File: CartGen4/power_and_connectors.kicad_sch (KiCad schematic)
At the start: 34 parts, among them J2 Conn_01x06_Male, U1 TPS65266-1RHBR

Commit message: Forgot to close footprint assignment tool
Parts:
- J2: footprint SamacSys_Parts:Pads_1x6_P2.54mm -> (none)
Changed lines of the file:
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@@
     (property "Reference" "J2" (id 0) (at 43.815 162.56 0))
     (property "Value" "Conn_01x06_Male" (id 1) (at 43.815 165.1 0))
-    (property "Footprint" "SamacSys_Parts:Pads_1x6_P2.54mm" (id 2) (at 43.18 172.72 0)
+    (property "Footprint" "" (id 2) (at 43.18 172.72 0)
       (effects (font (size 1.27 1.27)) hide)
     )

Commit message: Made general component placement + fixed ADDR
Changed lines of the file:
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@@
     )
   )
-  (global_label "GB_ADDR_5V[0..7]" (shape input) (at 193.04 71.12 180) (fields_autoplaced)
+  (global_label "GB_DATA_5V[0..7]" (shape input) (at 193.04 71.12 180) (fields_autoplaced)
     (effects (font (size 1.27 1.27)) (justify right))
-    (property "Intersheet References" "${INTERSHEET_REFS}" (id 0) (at 173.6331 71.0406 0)
+    (property "Intersheet References" "${INTERSHEET_REFS}" (id 0) (at 174.1169 71.0406 0)
       (effects (font (size 1.27 1.27)) (justify right) hide)
     )

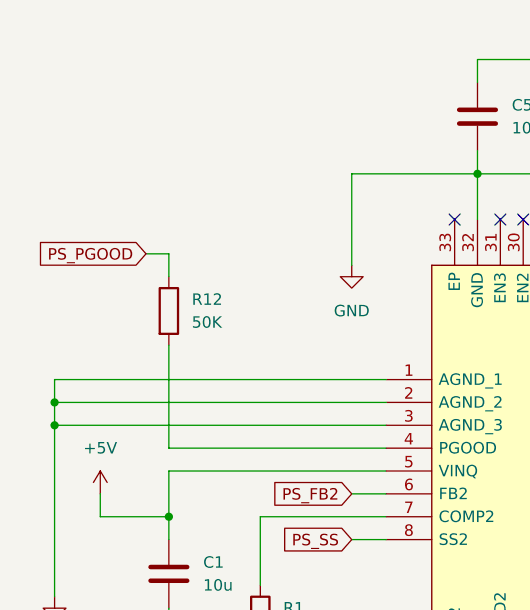
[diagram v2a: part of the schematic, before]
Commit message: Fixed PS_PGOOD pullup
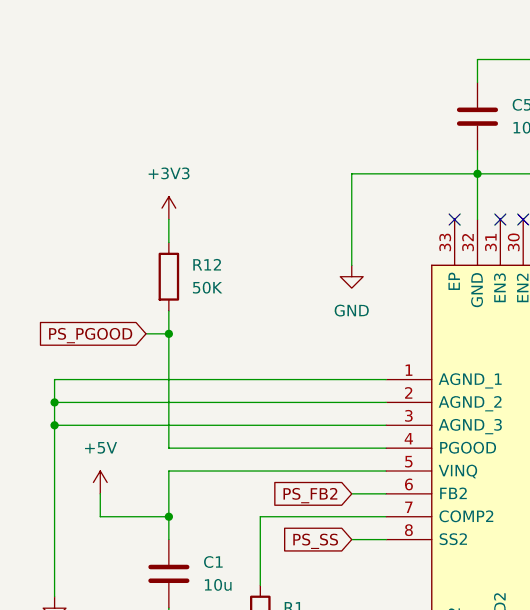
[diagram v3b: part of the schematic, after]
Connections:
- net +3V3: now also R12.1
- net PS_PGOOD: now also R12.2, U1.4 (PGOOD); no longer R12.1
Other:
- moved on the sheet: R12
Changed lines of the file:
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@@
   (junction (at 97.79 31.75) (diameter 0) (color 0 0 0 0)
+  )
+  (junction (at 43.18 62.23) (diameter 0) (color 0 0 0 0)
   )
   (junction (at 137.16 107.95) (diameter 0) (color 0 0 0 0)
@@
     (stroke (width 0) (type default) (color 0 0 0 0))
   )
-  (wire (pts (xy 43.18 74.93) (xy 43.18 63.5))
+  (wire (pts (xy 43.18 74.93) (xy 43.18 62.23))
     (stroke (width 0) (type default) (color 0 0 0 0))
   )
@@
     (stroke (width 0) (type default) (color 0 0 0 0))
   )
-  (wire (pts (xy 43.18 55.88) (xy 43.18 53.34))
-    (stroke (width 0) (type default) (color 0 0 0 0))
-  )
   (wire (pts (xy 120.65 41.91) (xy 120.65 44.45))
     (stroke (width 0) (type default) (color 0 0 0 0))
@@
     (stroke (width 0) (type default) (color 0 0 0 0))
   )
+  (wire (pts (xy 43.18 62.23) (xy 43.18 59.69))
+    (stroke (width 0) (type default) (color 0 0 0 0))
+  )
+  (wire (pts (xy 40.64 62.23) (xy 43.18 62.23))
+    (stroke (width 0) (type default) (color 0 0 0 0))
+  )
   (bus (pts (xy 217.17 82.55) (xy 217.17 80.01))
     (stroke (width 0) (type default) (color 0 0 0 0))
@@
     (stroke (width 0) (type default) (color 0 0 0 0))
   )
-  (wire (pts (xy 43.18 53.34) (xy 40.64 53.34))
-    (stroke (width 0) (type default) (color 0 0 0 0))
-  )
   (wire (pts (xy 212.09 123.19) (xy 247.65 123.19))
     (stroke (width 0) (type default) (color 0 0 0 0))
@@
   )
   (wire (pts (xy 102.87 80.01) (xy 106.68 80.01))
+    (stroke (width 0) (type default) (color 0 0 0 0))
+  )
+  (wire (pts (xy 43.18 49.53) (xy 43.18 52.07))
     (stroke (width 0) (type default) (color 0 0 0 0))
   )
@@
     )
   )
-  (global_label "PS_PGOOD" (shape input) (at 40.64 53.34 180) (fields_autoplaced)
+  (global_label "PS_PGOOD" (shape input) (at 40.64 62.23 180) (fields_autoplaced)
     (effects (font (size 1.27 1.27)) (justify right))
-    (property "Intersheet References" "${INTERSHEET_REFS}" (id 0) (at 28.3088 53.2606 0)
+    (property "Intersheet References" "${INTERSHEET_REFS}" (id 0) (at 28.3088 62.1506 0)
       (effects (font (size 1.27 1.27)) (justify right) hide)
     )
@@
     )
     (property "Datasheet" "" (id 3) (at 82.55 130.81 0)
+      (effects (font (size 1.27 1.27)) hide)
+    )
+    (pin "1")
+  )
+  (symbol (lib_id "power:+3V3") (at 43.18 49.53 0) (unit 1)
+    (in_bom yes) (on_board yes) (fields_autoplaced)
+    (property "Reference" "#PWR?" (id 0) (at 43.18 53.34 0)
+      (effects (font (size 1.27 1.27)) hide)
+    )
+    (property "Value" "+3V3" (id 1) (at 43.18 44.45 0))
+    (property "Footprint" "" (id 2) (at 43.18 49.53 0)
+      (effects (font (size 1.27 1.27)) hide)
+    )
+    (property "Datasheet" "" (id 3) (at 43.18 49.53 0)
       (effects (font (size 1.27 1.27)) hide)
     )
@@
     (pin "2")
   )
-  (symbol (lib_id "Device:R") (at 43.18 59.69 0) (unit 1)
+  (symbol (lib_id "Device:R") (at 43.18 55.88 0) (unit 1)
     (in_bom yes) (on_board yes) (fields_autoplaced)
-    (property "Reference" "R12" (id 0) (at 45.72 58.4199 0)
+    (property "Reference" "R12" (id 0) (at 45.72 54.6099 0)
       (effects (font (size 1.27 1.27)) (justify left))
     )
-    (property "Value" "50K" (id 1) (at 45.72 60.9599 0)
+    (property "Value" "50K" (id 1) (at 45.72 57.1499 0)
       (effects (font (size 1.27 1.27)) (justify left))
     )
-    (property "Footprint" "Resistor_SMD:R_0603_1608Metric_Pad0.98x0.95mm_HandSolder" (id 2) (at 41.402 59.69 90)
-      (effects (font (size 1.27 1.27)) hide)
-    )
-    (property "Datasheet" "~" (id 3) (at 43.18 59.69 0)
-      (effects (font (size 1.27 1.27)) hide)
-    )
-    (property "Tolerance" "10%" (id 4) (at 43.18 59.69 0)
-      (effects (font (size 1.27 1.27)) hide)
-    )
-    (property "Source" "ANY" (id 5) (at 43.18 59.69 0)
-      (effects (font (size 1.27 1.27)) hide)
-    )
-    (property "Critical" "Y" (id 6) (at 43.18 59.69 0)
-      (effects (font (size 1.27 1.27)) hide)
-    )
+    (property "Footprint" "Resistor_SMD:R_0603_1608Metric_Pad0.98x0.95mm_HandSolder" (id 2) (at 41.402 55.88 90)
+      (effects (font (size 1.27 1.27)) hide)
+    )
+    (property "Datasheet" "~" (id 3) (at 43.18 55.88 0)
+      (effects (font (size 1.27 1.27)) hide)
+    )
+    (property "Tolerance" "10%" (id 4) (at 43.18 55.88 0)
+      (effects (font (size 1.27 1.27)) hide)
+    )
+    (property "Source" "ANY" (id 5) (at 43.18 55.88 0)
+      (effects (font (size 1.27 1.27)) hide)
+    )
+    (property "Critical" "Y" (id 6) (at 43.18 55.88 0)
+      (effects (font (size 1.27 1.27)) hide)
+    )

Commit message: Changed most R and C to 0402 size
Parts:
- C11, C14, C17, C2, C3, C4, C9: footprint Capacitor_SMD:C_0603_1608Metric_Pad1.08x0.95mm_HandSolder -> Capacitor_SMD:C_0402_1005Metric_Pad0.74x0.62mm_HandSolder
- R1, R10, R12, R2, R3, R4, R5, R6, R7, R8, R9: footprint Resistor_SMD:R_0603_1608Metric_Pad0.98x0.95mm_HandSolder -> Resistor_SMD:R_0402_1005Metric_Pad0.72x0.64mm_HandSolder
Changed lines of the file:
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@@
       (effects (font (size 1.27 1.27)) (justify left))
     )
-    (property "Footprint" "Resistor_SMD:R_0603_1608Metric_Pad0.98x0.95mm_HandSolder" (id 2) (at 136.652 83.82 90)
+    (property "Footprint" "Resistor_SMD:R_0402_1005Metric_Pad0.72x0.64mm_HandSolder" (id 2) (at 136.652 83.82 90)
       (effects (font (size 1.27 1.27)) hide)
     )
@@
       (effects (font (size 1.27 1.27)) (justify left))
     )
-    (property "Footprint" "Capacitor_SMD:C_0603_1608Metric_Pad1.08x0.95mm_HandSolder" (id 2) (at 70.8152 115.57 0)
+    (property "Footprint" "Capacitor_SMD:C_0402_1005Metric_Pad0.74x0.62mm_HandSolder" (id 2) (at 70.8152 115.57 0)
       (effects (font (size 1.27 1.27)) hide)
     )
@@
       (effects (font (size 1.27 1.27)) (justify left))
     )
-    (property "Footprint" "Capacitor_SMD:C_0603_1608Metric_Pad1.08x0.95mm_HandSolder" (id 2) (at 110.1852 105.41 0)
+    (property "Footprint" "Capacitor_SMD:C_0402_1005Metric_Pad0.74x0.62mm_HandSolder" (id 2) (at 110.1852 105.41 0)
       (effects (font (size 1.27 1.27)) hide)
     )
@@
   (symbol (lib_id "power:+3V3") (at 43.18 49.53 0) (unit 1)
     (in_bom yes) (on_board yes) (fields_autoplaced)
-    (property "Reference" "#PWR?" (id 0) (at 43.18 53.34 0)
+    (property "Reference" "#PWR0102" (id 0) (at 43.18 53.34 0)
       (effects (font (size 1.27 1.27)) hide)
     )
@@
       (effects (font (size 1.27 1.27)) (justify left))
     )
-    (property "Footprint" "Resistor_SMD:R_0603_1608Metric_Pad0.98x0.95mm_HandSolder" (id 2) (at 130.302 50.8 90)
+    (property "Footprint" "Resistor_SMD:R_0402_1005Metric_Pad0.72x0.64mm_HandSolder" (id 2) (at 130.302 50.8 90)
       (effects (font (size 1.27 1.27)) hide)
     )
@@
       (effects (font (size 1.27 1.27)) (justify left))
     )
-    (property "Footprint" "Resistor_SMD:R_0603_1608Metric_Pad0.98x0.95mm_HandSolder" (id 2) (at 41.402 55.88 90)
+    (property "Footprint" "Resistor_SMD:R_0402_1005Metric_Pad0.72x0.64mm_HandSolder" (id 2) (at 41.402 55.88 90)
       (effects (font (size 1.27 1.27)) hide)
     )
@@
       (effects (font (size 1.27 1.27)) (justify left))
     )
-    (property "Footprint" "Capacitor_SMD:C_0603_1608Metric_Pad1.08x0.95mm_HandSolder" (id 2) (at 129.2352 92.71 0)
+    (property "Footprint" "Capacitor_SMD:C_0402_1005Metric_Pad0.74x0.62mm_HandSolder" (id 2) (at 129.2352 92.71 0)
       (effects (font (size 1.27 1.27)) hide)
     )
@@
     (property "Reference" "R8" (id 0) (at 147.32 63.5 90))
     (property "Value" "39K" (id 1) (at 147.32 66.04 90))
-    (property "Footprint" "Resistor_SMD:R_0603_1608Metric_Pad0.98x0.95mm_HandSolder" (id 2) (at 147.32 71.628 90)
+    (property "Footprint" "Resistor_SMD:R_0402_1005Metric_Pad0.72x0.64mm_HandSolder" (id 2) (at 147.32 71.628 90)
       (effects (font (size 1.27 1.27)) hide)
     )
@@
       (effects (font (size 1.27 1.27)) (justify left))
     )
-    (property "Footprint" "Capacitor_SMD:C_0603_1608Metric_Pad1.08x0.95mm_HandSolder" (id 2) (at 44.1452 135.89 0)
+    (property "Footprint" "Capacitor_SMD:C_0402_1005Metric_Pad0.74x0.62mm_HandSolder" (id 2) (at 44.1452 135.89 0)
       (effects (font (size 1.27 1.27)) hide)
     )
@@
       (effects (font (size 1.27 1.27)) (justify left))
     )
-    (property "Footprint" "Capacitor_SMD:C_0603_1608Metric_Pad1.08x0.95mm_HandSolder" (id 2) (at 154.6352 80.01 0)
+    (property "Footprint" "Capacitor_SMD:C_0402_1005Metric_Pad0.74x0.62mm_HandSolder" (id 2) (at 154.6352 80.01 0)
       (effects (font (size 1.27 1.27)) hide)
     )
@@
       (effects (font (size 1.27 1.27)) (justify left))
     )
-    (property "Footprint" "Capacitor_SMD:C_0603_1608Metric_Pad1.08x0.95mm_HandSolder" (id 2) (at 54.3052 107.95 0)
+    (property "Footprint" "Capacitor_SMD:C_0402_1005Metric_Pad0.74x0.62mm_HandSolder" (id 2) (at 54.3052 107.95 0)
       (effects (font (size 1.27 1.27)) hide)
     )
@@
       (effects (font (size 1.27 1.27)) (justify left))
     )
-    (property "Footprint" "Resistor_SMD:R_0603_1608Metric_Pad0.98x0.95mm_HandSolder" (id 2) (at 130.302 38.1 90)
+    (property "Footprint" "Resistor_SMD:R_0402_1005Metric_Pad0.72x0.64mm_HandSolder" (id 2) (at 130.302 38.1 90)
       (effects (font (size 1.27 1.27)) hide)
     )
@@
       (effects (font (size 1.27 1.27)) (justify left))
     )
-    (property "Footprint" "Resistor_SMD:R_0603_1608Metric_Pad0.98x0.95mm_HandSolder" (id 2) (at 156.972 114.3 90)
+    (property "Footprint" "Resistor_SMD:R_0402_1005Metric_Pad0.72x0.64mm_HandSolder" (id 2) (at 156.972 114.3 90)
       (effects (font (size 1.27 1.27)) hide)
     )
@@
     (property "Reference" "R4" (id 0) (at 121.92 85.09 90))
     (property "Value" "100K" (id 1) (at 121.92 87.63 90))
-    (property "Footprint" "Resistor_SMD:R_0603_1608Metric_Pad0.98x0.95mm_HandSolder" (id 2) (at 121.92 84.328 90)
+    (property "Footprint" "Resistor_SMD:R_0402_1005Metric_Pad0.72x0.64mm_HandSolder" (id 2) (at 121.92 84.328 90)
       (effects (font (size 1.27 1.27)) hide)
     )
@@
       (effects (font (size 1.27 1.27)) (justify left))
     )
-    (property "Footprint" "Resistor_SMD:R_0603_1608Metric_Pad0.98x0.95mm_HandSolder" (id 2) (at 113.792 158.75 90)
+    (property "Footprint" "Resistor_SMD:R_0402_1005Metric_Pad0.72x0.64mm_HandSolder" (id 2) (at 113.792 158.75 90)
       (effects (font (size 1.27 1.27)) hide)
     )
@@
       (effects (font (size 1.27 1.27)) (justify left))
     )
-    (property "Footprint" "Capacitor_SMD:C_0603_1608Metric_Pad1.08x0.95mm_HandSolder" (id 2) (at 98.7552 41.91 0)
+    (property "Footprint" "Capacitor_SMD:C_0402_1005Metric_Pad0.74x0.62mm_HandSolder" (id 2) (at 98.7552 41.91 0)
       (effects (font (size 1.27 1.27)) hide)
     )
@@
       (effects (font (size 1.27 1.27)) (justify left))
     )
-    (property "Footprint" "Resistor_SMD:R_0603_1608Metric_Pad0.98x0.95mm_HandSolder" (id 2) (at 51.562 93.98 90)
+    (property "Footprint" "Resistor_SMD:R_0402_1005Metric_Pad0.72x0.64mm_HandSolder" (id 2) (at 51.562 93.98 90)
       (effects (font (size 1.27 1.27)) hide)
     )
@@
       (effects (font (size 1.27 1.27)) (justify left))
     )
-    (property "Footprint" "Resistor_SMD:R_0603_1608Metric_Pad0.98x0.95mm_HandSolder" (id 2) (at 113.792 146.05 90)
+    (property "Footprint" "Resistor_SMD:R_0402_1005Metric_Pad0.72x0.64mm_HandSolder" (id 2) (at 113.792 146.05 90)
       (effects (font (size 1.27 1.27)) hide)
     )
@@
       (effects (font (size 1.27 1.27)) (justify left))
     )
-    (property "Footprint" "Resistor_SMD:R_0603_1608Metric_Pad0.98x0.95mm_HandSolder" (id 2) (at 156.972 127 90)
-      (effects (font (size 1.27 1.27)) hide)
-    )
+    (property "Footprint" "Resistor_SMD:R_0402_1005Metric_Pad0.72x0.64mm_HandSolder" (id 2) (at 156.972 127 90)
+      (effects (font (size 1.27 1.27)) hide)
+    )

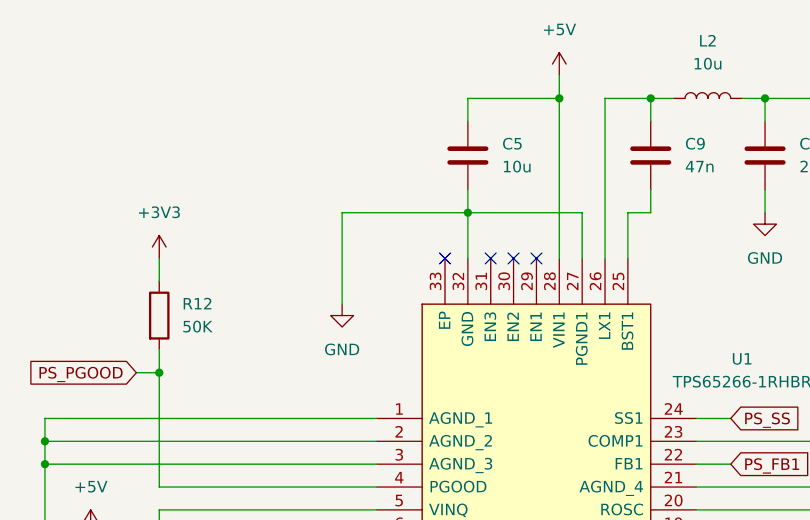
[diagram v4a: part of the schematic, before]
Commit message: Wired power supply
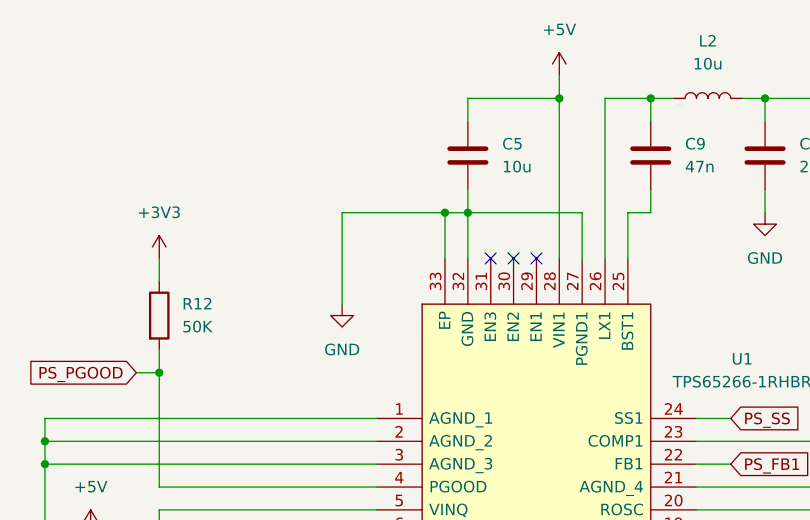
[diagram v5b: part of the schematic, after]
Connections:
- net GND: now also U1.33 (EP)
- no-connect marks 6 -> 5
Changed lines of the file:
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@@
   (junction (at 132.08 31.75) (diameter 0) (color 0 0 0 0)
+  )
+  (junction (at 74.93 44.45) (diameter 0) (color 0 0 0 0)
   )
   (junction (at 43.18 82.55) (diameter 0) (color 0 0 0 0)
@@
   (no_connect (at 80.01 49.53))
   (no_connect (at 85.09 49.53))
-  (no_connect (at 74.93 49.53))
   (no_connect (at 48.26 167.64))
   (bus_entry (at 217.17 82.55) (size 2.54 2.54)
@@
     (stroke (width 0) (type default) (color 0 0 0 0))
   )
+  (wire (pts (xy 74.93 44.45) (xy 63.5 44.45))
+    (stroke (width 0) (type default) (color 0 0 0 0))
+  )
   (wire (pts (xy 241.3 133.35) (xy 247.65 133.35))
     (stroke (width 0) (type default) (color 0 0 0 0))
@@
     (stroke (width 0) (type default) (color 0 0 0 0))
   )
-  (wire (pts (xy 77.47 44.45) (xy 63.5 44.45))
+  (wire (pts (xy 77.47 44.45) (xy 74.93 44.45))
     (stroke (width 0) (type default) (color 0 0 0 0))
   )
@@
     (stroke (width 0) (type default) (color 0 0 0 0))
   )
+  (wire (pts (xy 74.93 44.45) (xy 74.93 49.53))
+    (stroke (width 0) (type default) (color 0 0 0 0))
+  )

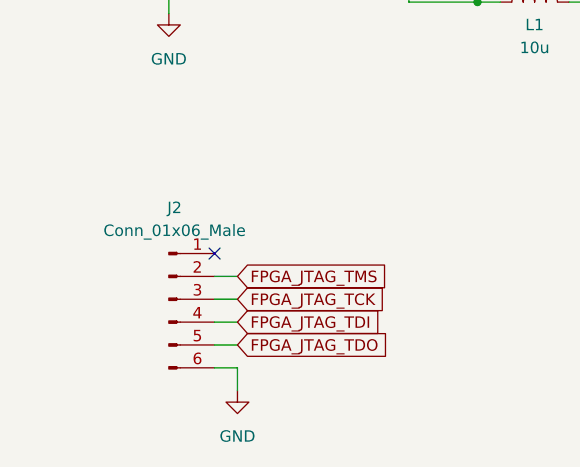
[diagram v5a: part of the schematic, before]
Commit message: Wired general purpose signals
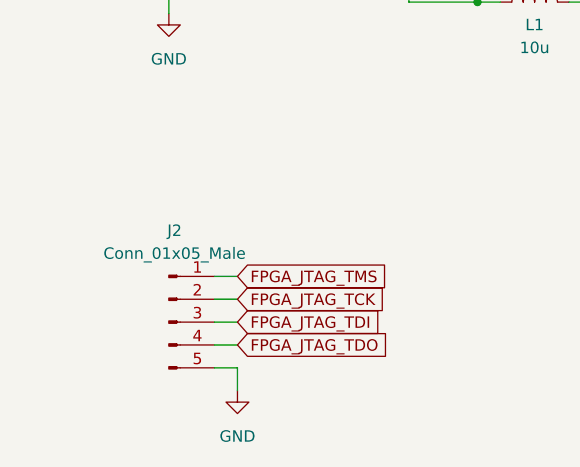
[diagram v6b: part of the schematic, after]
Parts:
- removed J2: Conn_01x06_Male, symbol Connector:Conn_01x06_Male
- added J2: Conn_01x05_Male, Connector_PinHeader_2.54mm:PinHeader_1x05_P2.54mm_Horizontal, symbol Connector:Conn_01x05_Male
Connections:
- net FPGA_JTAG_TCK: now also J2.2 (Pin_2)
- net FPGA_JTAG_TDI: now also J2.3 (Pin_3)
- net FPGA_JTAG_TDO: now also J2.4 (Pin_4)
- net FPGA_JTAG_TMS: now also J2.1 (Pin_1)
- net GND: now also J2.5 (Pin_5)
- no-connect marks 5 -> 4
